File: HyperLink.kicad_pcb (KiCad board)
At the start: 2 copper layers, 35 x 24 mm, 45 parts, among them J1 USB_C_Receptacle_USB2.0, J2 Conn_02x05_Odd_Even, J3 Conn_02x05_Odd_Even, SW1 SW_Push, U1 ESP32-C3, U2 PESD2USB5UXT, U3 MIC5504-3.3YM5, Y1 ABM11W-40.0000MHZ-8-B1U-T3

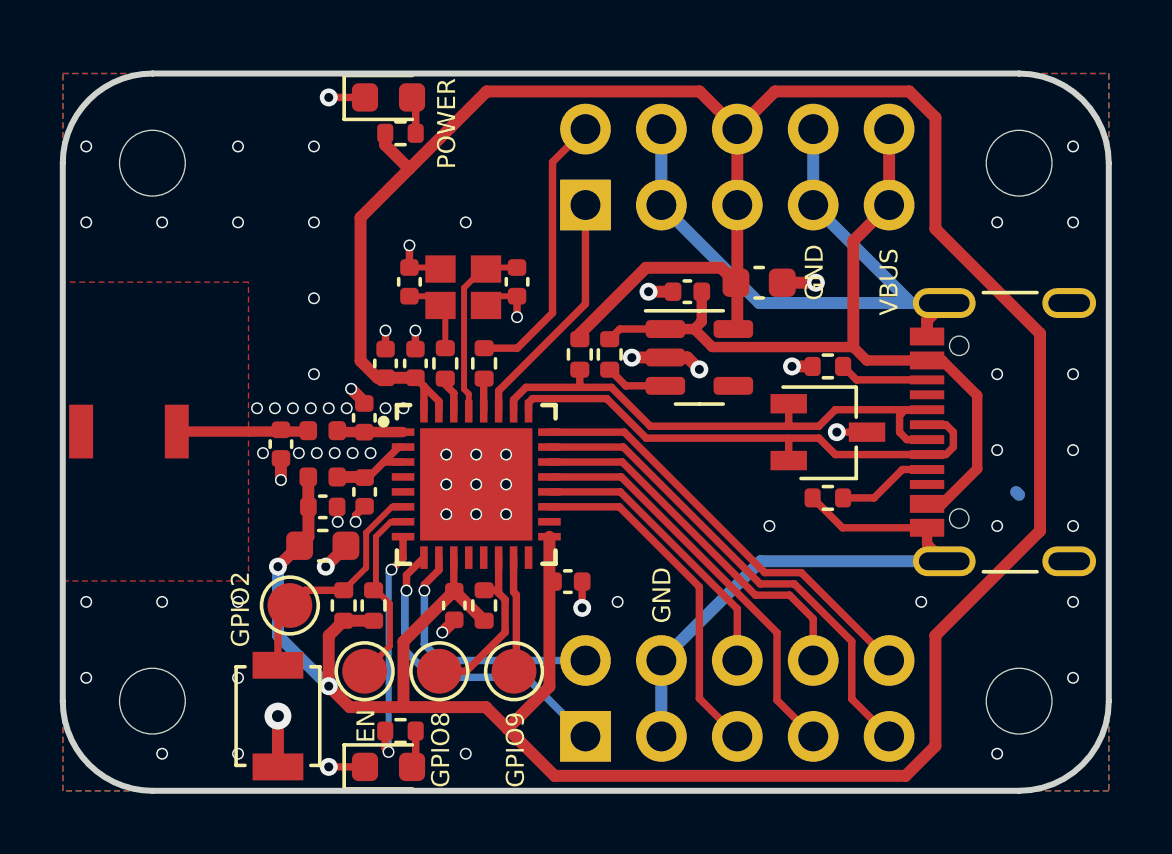
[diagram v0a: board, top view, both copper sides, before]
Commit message: Check out new version of library and replace usb connector footprint
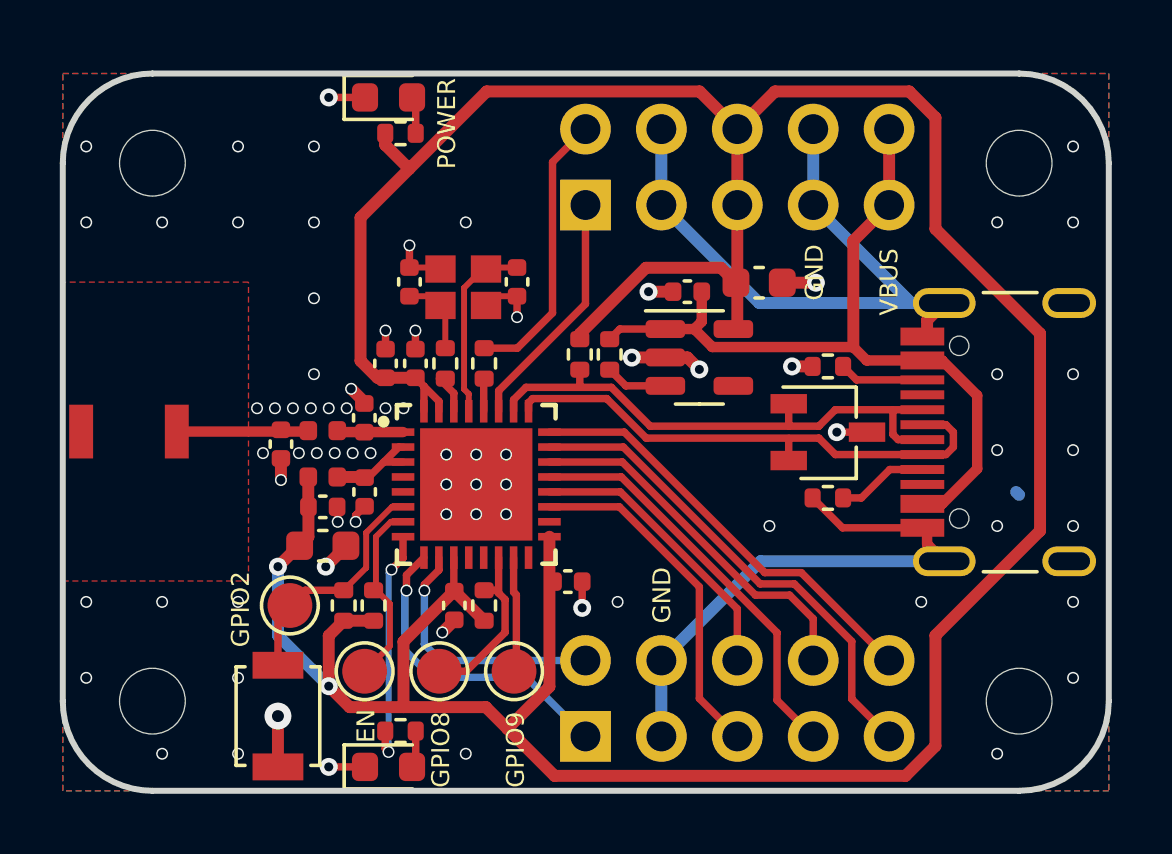
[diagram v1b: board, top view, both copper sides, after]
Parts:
- J1: footprint Connector_USB:USB_C_Receptacle_GCT_USB4105-xx-A_16P_TopMnt_Horizontal -> encyclopedia_galactica:USB4105-GF-A
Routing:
- net /USB_D+: track 19.1 -> 18.2 mm
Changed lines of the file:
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@@
     )
   )
-  (footprint "Connector_USB:USB_C_Receptacle_GCT_USB4105-xx-A_16P_TopMnt_Horizontal" locked (layer "F.Cu")
+  (footprint "encyclopedia_galactica:USB4105-GF-A" locked (layer "F.Cu")
     (at 151.6 82 90)
     (descr "USB 2.0 Type C Receptacle, GCT, 16P, top mounted, horizontal, 5A: https://gct.co/files/drawings/usb4105.pdf")
@@
     (pad "" np_thru_hole circle locked (at -2.89 -2.605 90) (size 0.65 0.65) (drill 0.65) (layers "F&B.Cu" "*.Mask"))
     (pad "" np_thru_hole circle locked (at 2.89 -2.605 90) (size 0.65 0.65) (drill 0.65) (layers "F&B.Cu" "*.Mask"))
-    (pad "A1" smd rect locked (at -3.2 -3.68 90) (size 0.6 1.15) (layers "F.Cu" "F.Paste" "F.Mask")
+    (pad "A1" smd rect locked (at -3.2 -3.8385 90) (size 0.6 1.467) (layers "F.Cu" "F.Paste" "F.Mask")
       (net 5 "GND") (pinfunction "GND") (pintype "passive"))
-    (pad "A4" smd rect locked (at -2.4 -3.68 90) (size 0.6 1.15) (layers "F.Cu" "F.Paste" "F.Mask")
+    (pad "A4" smd rect locked (at -2.4 -3.8385 90) (size 0.6 1.467) (layers "F.Cu" "F.Paste" "F.Mask")
       (net 4 "VBUS") (pinfunction "VBUS") (pintype "passive"))
-    (pad "A5" smd rect locked (at -1.25 -3.68 90) (size 0.3 1.15) (layers "F.Cu" "F.Paste" "F.Mask")
+    (pad "A5" smd rect locked (at -1.25 -3.8385 90) (size 0.3 1.467) (layers "F.Cu" "F.Paste" "F.Mask")
       (net 35 "/CC1") (pinfunction "CC1") (pintype "bidirectional"))
-    (pad "A6" smd rect locked (at -0.25 -3.68 90) (size 0.3 1.15) (layers "F.Cu" "F.Paste" "F.Mask")
+    (pad "A6" smd rect locked (at -0.25 -3.8385 90) (size 0.3 1.467) (layers "F.Cu" "F.Paste" "F.Mask")
       (net 12 "/USB_D+") (pinfunction "D+") (pintype "bidirectional"))
-    (pad "A7" smd rect locked (at 0.25 -3.68 90) (size 0.3 1.15) (layers "F.Cu" "F.Paste" "F.Mask")
+    (pad "A7" smd rect locked (at 0.25 -3.8385 90) (size 0.3 1.467) (layers "F.Cu" "F.Paste" "F.Mask")
       (net 11 "/USB_D-") (pinfunction "D-") (pintype "bidirectional"))
-    (pad "A8" smd rect locked (at 1.25 -3.68 90) (size 0.3 1.15) (layers "F.Cu" "F.Paste" "F.Mask")
+    (pad "A8" smd rect locked (at 1.25 -3.8385 90) (size 0.3 1.467) (layers "F.Cu" "F.Paste" "F.Mask")
       (net 2 "unconnected-(J1-SBU1-PadA8)") (pinfunction "SBU1") (pintype "bidirectional+no_connect"))
-    (pad "A9" smd rect locked (at 2.4 -3.68 90) (size 0.6 1.15) (layers "F.Cu" "F.Paste" "F.Mask")
+    (pad "A9" smd rect locked (at 2.4 -3.8385 90) (size 0.6 1.467) (layers "F.Cu" "F.Paste" "F.Mask")
       (net 4 "VBUS") (pinfunction "VBUS") (pintype "passive"))
-    (pad "A12" smd rect locked (at 3.2 -3.68 90) (size 0.6 1.15) (layers "F.Cu" "F.Paste" "F.Mask")
+    (pad "A12" smd rect locked (at 3.2 -3.8385 90) (size 0.6 1.467) (layers "F.Cu" "F.Paste" "F.Mask")
       (net 5 "GND") (pinfunction "GND") (pintype "passive"))
-    (pad "B1" smd rect locked (at 3.2 -3.68 90) (size 0.6 1.15) (layers "F.Cu" "F.Paste" "F.Mask")
+    (pad "B1" smd rect locked (at 3.2 -3.8385 90) (size 0.6 1.467) (layers "F.Cu" "F.Paste" "F.Mask")
       (net 5 "GND") (pinfunction "GND") (pintype "passive"))
-    (pad "B4" smd rect locked (at 2.4 -3.68 90) (size 0.6 1.15) (layers "F.Cu" "F.Paste" "F.Mask")
+    (pad "B4" smd rect locked (at 2.4 -3.8385 90) (size 0.6 1.467) (layers "F.Cu" "F.Paste" "F.Mask")
       (net 4 "VBUS") (pinfunction "VBUS") (pintype "passive"))
-    (pad "B5" smd rect locked (at 1.75 -3.68 90) (size 0.3 1.15) (layers "F.Cu" "F.Paste" "F.Mask")
+    (pad "B5" smd rect locked (at 1.75 -3.8385 90) (size 0.3 1.467) (layers "F.Cu" "F.Paste" "F.Mask")
       (net 36 "/CC2") (pinfunction "CC2") (pintype "bidirectional"))
-    (pad "B6" smd rect locked (at 0.75 -3.68 90) (size 0.3 1.15) (layers "F.Cu" "F.Paste" "F.Mask")
+    (pad "B6" smd rect locked (at 0.75 -3.8385 90) (size 0.3 1.467) (layers "F.Cu" "F.Paste" "F.Mask")
       (net 12 "/USB_D+") (pinfunction "D+") (pintype "bidirectional"))
-    (pad "B7" smd rect locked (at -0.75 -3.68 90) (size 0.3 1.15) (layers "F.Cu" "F.Paste" "F.Mask")
+    (pad "B7" smd rect locked (at -0.75 -3.8385 90) (size 0.3 1.467) (layers "F.Cu" "F.Paste" "F.Mask")
       (net 11 "/USB_D-") (pinfunction "D-") (pintype "bidirectional"))
-    (pad "B8" smd rect locked (at -1.75 -3.68 90) (size 0.3 1.15) (layers "F.Cu" "F.Paste" "F.Mask")
+    (pad "B8" smd rect locked (at -1.75 -3.8385 90) (size 0.3 1.467) (layers "F.Cu" "F.Paste" "F.Mask")
       (net 3 "unconnected-(J1-SBU2-PadB8)") (pinfunction "SBU2") (pintype "bidirectional+no_connect"))
-    (pad "B9" smd rect locked (at -2.4 -3.68 90) (size 0.6 1.15) (layers "F.Cu" "F.Paste" "F.Mask")
+    (pad "B9" smd rect locked (at -2.4 -3.8385 90) (size 0.6 1.467) (layers "F.Cu" "F.Paste" "F.Mask")
       (net 4 "VBUS") (pinfunction "VBUS") (pintype "passive"))
-    (pad "B12" smd rect locked (at -3.2 -3.68 90) (size 0.6 1.15) (layers "F.Cu" "F.Paste" "F.Mask")
+    (pad "B12" smd rect locked (at -3.2 -3.8385 90) (size 0.6 1.467) (layers "F.Cu" "F.Paste" "F.Mask")
       (net 5 "GND") (pinfunction "GND") (pintype "passive"))
     (pad "S1" thru_hole oval locked (at -4.32 -3.105 90) (size 1 2.1) (drill oval 0.6 1.7) (layers "*.Cu" "*.Mask" "F.Paste")
@@
   (segment (start 134.723 80.877) (end 137.200684 80.877) (width 0.25) (layer "F.Cu") (net 11))
   (segment (start 143.29 82.21) (end 143.29 82.95) (width 0.25) (layer "F.Cu") (net 11))
-  (segment (start 147.245 82.25) (end 147.92 82.25) (width 0.25) (layer "F.Cu") (net 12))
+  (segment (start 144.3 81.8) (end 144.85 81.25) (width 0.25) (layer "F.Cu") (net 12))
+  (segment (start 144.85 81.25) (end 147.7615 81.25) (width 0.25) (layer "F.Cu") (net 12))
   (segment (start 138.656842 81.8) (end 144.3 81.8) (width 0.25) (layer "F.Cu") (net 12))
   (segment (start 143.29 81.79) (end 143.29 81.05) (width 0.25) (layer "F.Cu") (net 12))
-  (segment (start 147 82.005) (end 147.245 82.25) (width 0.25) (layer "F.Cu") (net 12))
+  (segment (start 147.7615 82.25) (end 146.95 82.25) (width 0.25) (layer "F.Cu") (net 12))
+  (segment (start 136.3 80.5) (end 137.356842 80.5) (width 0.25) (layer "F.Cu") (net 12))
+  (segment (start 134.084851 80.915149) (end 134.084851 81.3) (width 0.25) (layer "F.Cu") (net 12))
+  (segment (start 134.5 80.5) (end 134.084851 80.915149) (width 0.25) (layer "F.Cu") (net 12))
   (segment (start 137.356842 80.5) (end 138.656842 81.8) (width 0.25) (layer "F.Cu") (net 12))
-  (segment (start 144.3 81.8) (end 144.85 81.25) (width 0.25) (layer "F.Cu") (net 12))
-  (segment (start 134.084851 80.915149) (end 134.084851 81.3) (width 0.25) (layer "F.Cu") (net 12))
-  (segment (start 136.3 80.5) (end 137.356842 80.5) (width 0.25) (layer "F.Cu") (net 12))
-  (segment (start 144.85 81.25) (end 147.92 81.25) (width 0.25) (layer "F.Cu") (net 12))
-  (segment (start 134.5 80.5) (end 134.084851 80.915149) (width 0.25) (layer "F.Cu") (net 12))
-  (segment (start 147.191 81.25) (end 147 81.441) (width 0.25) (layer "F.Cu") (net 12))
+  (segment (start 146.776 82.076) (end 146.776 81.274) (width 0.25) (layer "F.Cu") (net 12))
   (segment (start 136.3 79.91) (end 136.3 80.5) (width 0.25) (layer "F.Cu") (net 12))
-  (segment (start 147 81.441) (end 147 82.005) (width 0.25) (layer "F.Cu") (net 12))
-  (segment (start 147.92 81.25) (end 147.191 81.25) (width 0.25) (layer "F.Cu") (net 12))
   (segment (start 136.3 80.5) (end 134.5 80.5) (width 0.25) (layer "F.Cu") (net 12))
+  (segment (start 146.95 82.25) (end 146.776 82.076) (width 0.25) (layer "F.Cu") (net 12))
   (segment (start 134.084851 86.1974) (end 134.084851 87.351692) (width 0.25) (layer "F.Cu") (net 14))
   (segment (start 134.177 87.443841) (end 134.177 89.923) (width 0.25) (layer "F.Cu") (net 14))
@@
   (segment (start 131.099503 89.099503) (end 131.64 89.64) (width 0.25) (layer "B.Cu") (net 33))
   (segment (start 133.084851 81.3) (end 133.084851 80.365149) (width 0.25) (layer "F.Cu") (net 34))
-  (segment (start 147.92 83.25) (end 147.095 83.25) (width 0.25) (layer "F.Cu") (net 35))
-  (segment (start 146.145 84.2) (end 145.11 84.2) (width 0.25) (layer "F.Cu") (net 35))
-  (segment (start 147.095 83.25) (end 146.145 84.2) (width 0.25) (layer "F.Cu") (net 35))
+  (segment (start 145.7225 84.2) (end 145.11 84.2) (width 0.25) (layer "F.Cu") (net 35))
+  (segment (start 147.92 83.25) (end 146.6725 83.25) (width 0.25) (layer "F.Cu") (net 35))
+  (segment (start 146.6725 83.25) (end 145.7225 84.2) (width 0.25) (layer "F.Cu") (net 35))
   (segment (start 145.56 80.25) (end 147.92 80.25) (width 0.25) (layer "F.Cu") (net 36))
   (segment (start 145.11 79.8) (end 145.56 80.25) (width 0.25) (layer "F.Cu") (net 36))

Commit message: Fix matching network component values
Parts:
- C1: value 4.7p -> 4p5
- C14: value 4p -> 3p9
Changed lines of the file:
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@@
         (effects (font (size 1 1) (thickness 0.15)))
     )
-    (fp_text value "4p" (at 0 1.16 90) (layer "F.Fab") hide
+    (fp_text value "3p9" (at 0 1.16 90) (layer "F.Fab") hide
         (effects (font (size 1 1) (thickness 0.15)))
     )
@@
         (effects (font (size 1 1) (thickness 0.15)))
     )
-    (fp_text value "4.7p" (at 0 1.16 90) (layer "F.Fab") hide
+    (fp_text value "4p5" (at 0 1.16 90) (layer "F.Fab") hide
         (effects (font (size 1 1) (thickness 0.15)))
     )

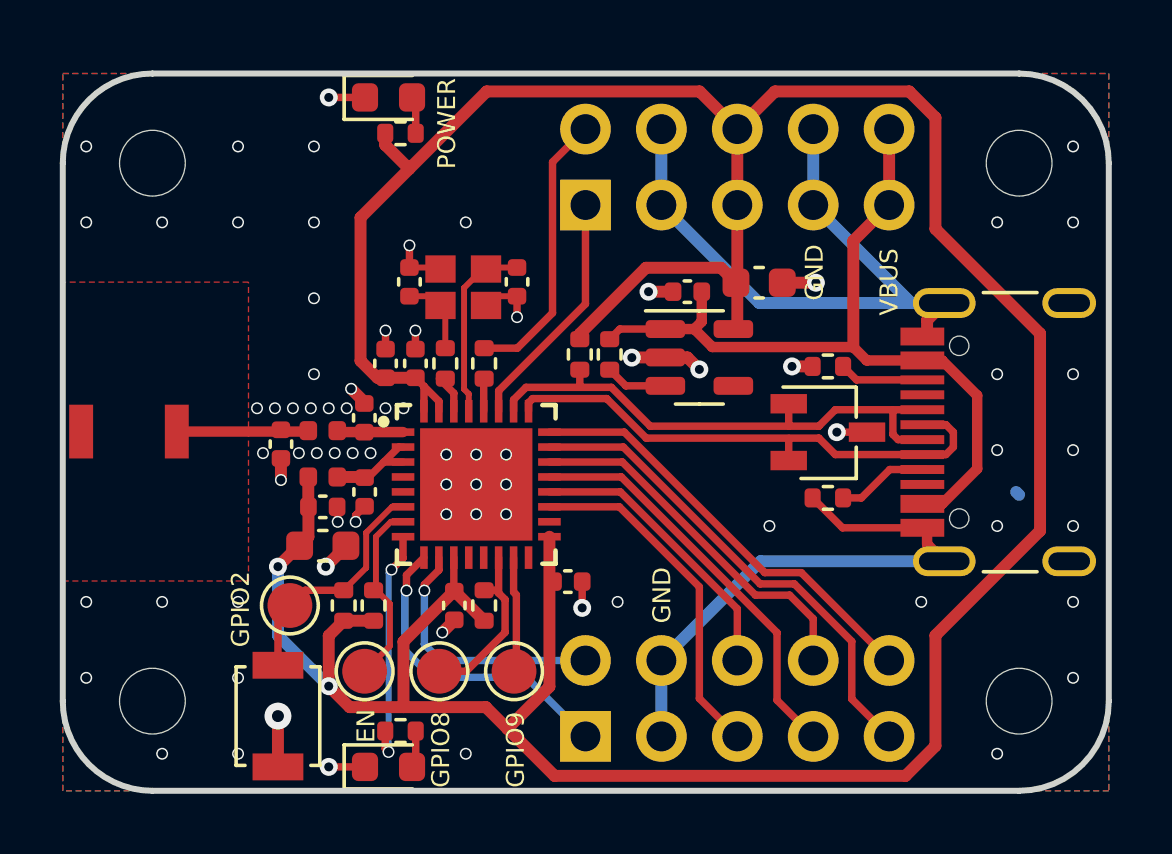
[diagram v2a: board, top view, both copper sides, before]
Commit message: Add pulldown resistor to GPIO9 pin
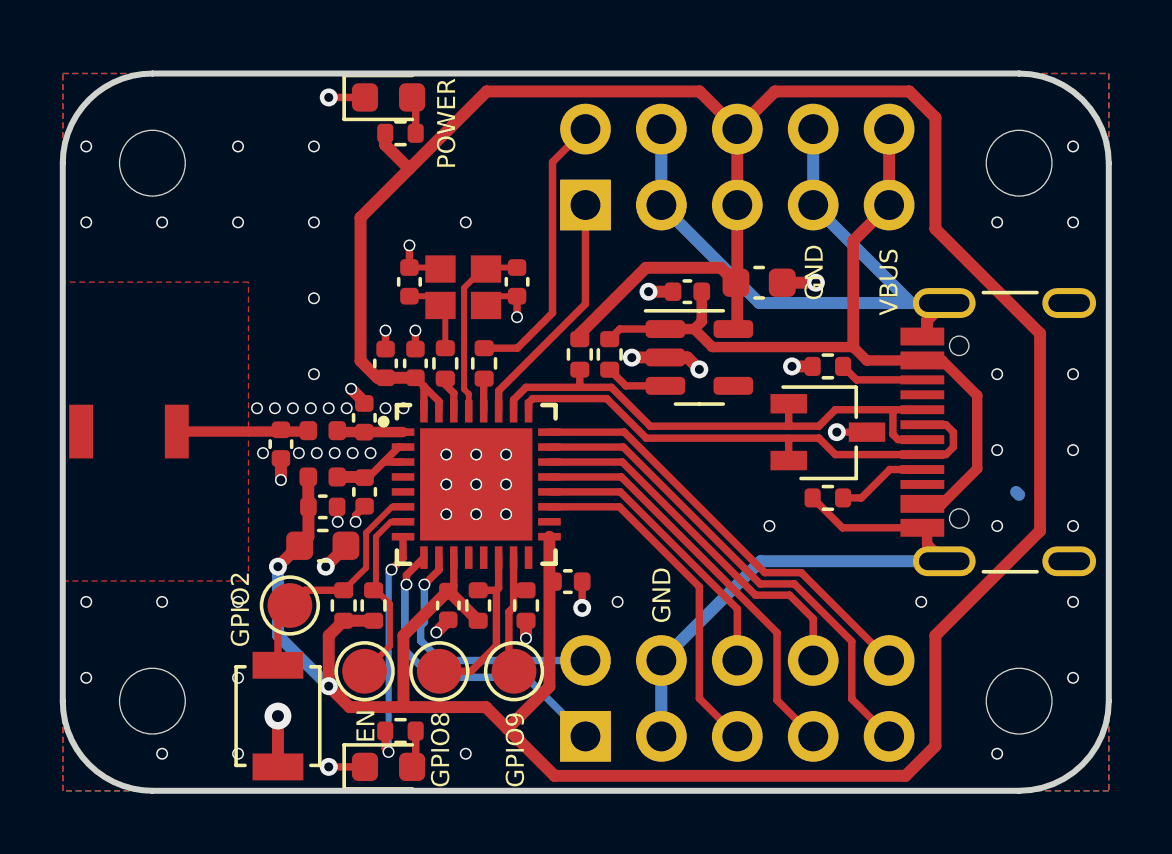
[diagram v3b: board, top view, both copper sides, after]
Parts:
- added R9: 10k, Resistor_SMD:R_0402_1005Metric, F.Cu at (134.5, 87.8)
- moved C17 0.20 mm to (131.9, 87.8)
- moved R2 0.20 mm to (132.9, 87.8)
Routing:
- net GND: track 62.3 -> 62.9 mm, vias 76 -> 77
